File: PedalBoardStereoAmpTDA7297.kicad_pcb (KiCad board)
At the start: 2 copper layers, 49.5 x 27.9 mm, 17 parts, among them J1 OUT-L, J2 IN-L, J3 OUT-R, J4 IN-R, J5 PWR, U1 TDA7297

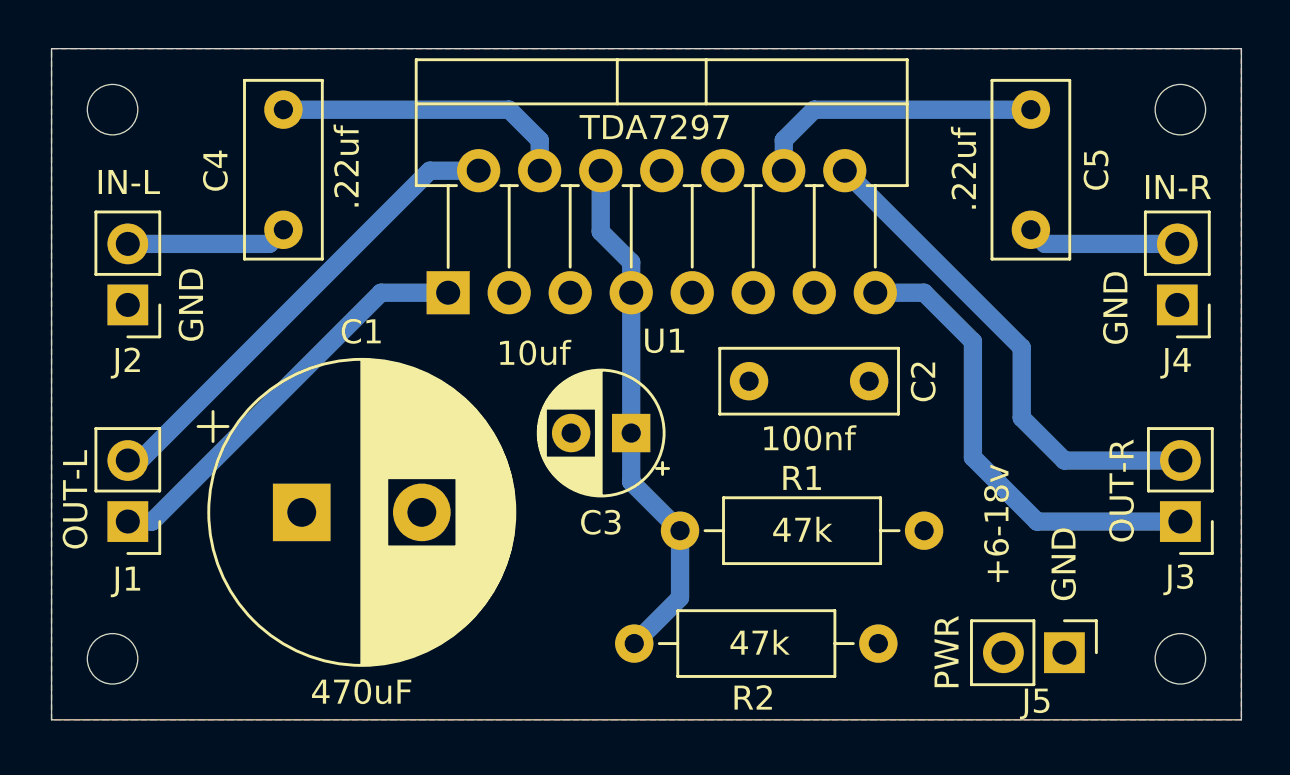
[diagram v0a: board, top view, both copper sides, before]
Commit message: update with pots connector
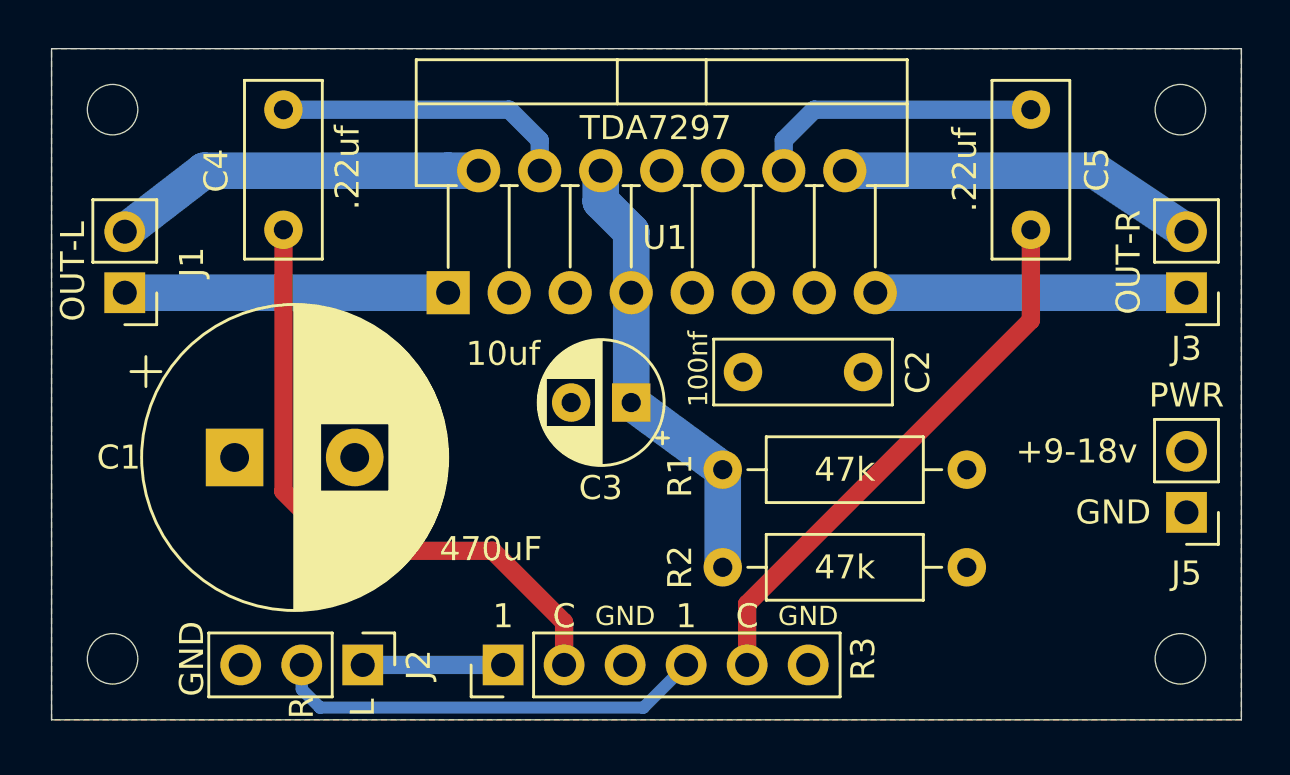
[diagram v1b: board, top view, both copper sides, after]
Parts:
- removed J4: IN-R, Connector_PinHeader_2.54mm:PinHeader_1x02_P2.54mm_Vertical
- added R3: 50k, Connector_PinHeader_2.54mm:PinHeader_1x06_P2.54mm_Vertical, F.Cu at (79.8, 61.2)
- J2: value IN-L -> Conn_01x03_Male; footprint Connector_PinHeader_2.54mm:PinHeader_1x02_P2.54mm_Vertical -> Connector_PinHeader_2.54mm:PinHeader_1x03_P2.54mm_Vertical
- moved J2 17.9 mm to (73.9, 61.2), turned to 270 degrees
- moved J3 9.53 mm to (108.2, 45.7)
- moved J1 9.53 mm to (64.0, 45.7)
- moved J5 7.74 mm to (108.2, 54.9), turned to 180 degrees
- moved R2 4.86 mm to (88.9, 57.1)
- moved C1 3.61 mm to (68.6, 52.6)
- moved R1 3.10 mm to (99.1, 53.1)
- moved C3 1.27 mm to (85.1, 50.3)
- moved C2 0.46 mm to (94.7, 49.0)
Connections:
- J2 pad 1: GND -> Net-(J2-Pad1)
- J2 pad 2: Net-(C4-Pad2) -> Net-(J2-Pad2)
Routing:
- net Net-(C4-Pad2): track 6.72 -> 27.0 mm
- net Net-(J2-Pad2): track 0.00 -> 18.1 mm
- net Net-(C5-Pad2): track 6.34 -> 23.0 mm
- net Net-(J3-Pad1): track 19.5 -> 13.0 mm
- net Net-(J2-Pad1): track 0.00 -> 5.84 mm
- net Net-(J3-Pad2): track 20.7 -> 15.0 mm
- net Net-(J1-Pad2): track 19.6 -> 15.6 mm
- net Net-(J1-Pad1): track 17.3 -> 13.5 mm
- net Net-(C3-Pad1): track 21.8 -> 18.7 mm
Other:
- board text added: "+9-18v"
- board text added: "1"
- board text added: "C"
- board text added: "L"
- board text added: "R"
- board text removed: "+6-18v"
